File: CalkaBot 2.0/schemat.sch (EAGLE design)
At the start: 63 parts, among them IC1 TB6612FNG, IC2 LM339D, IC3 7806DT, Q1 16MHz

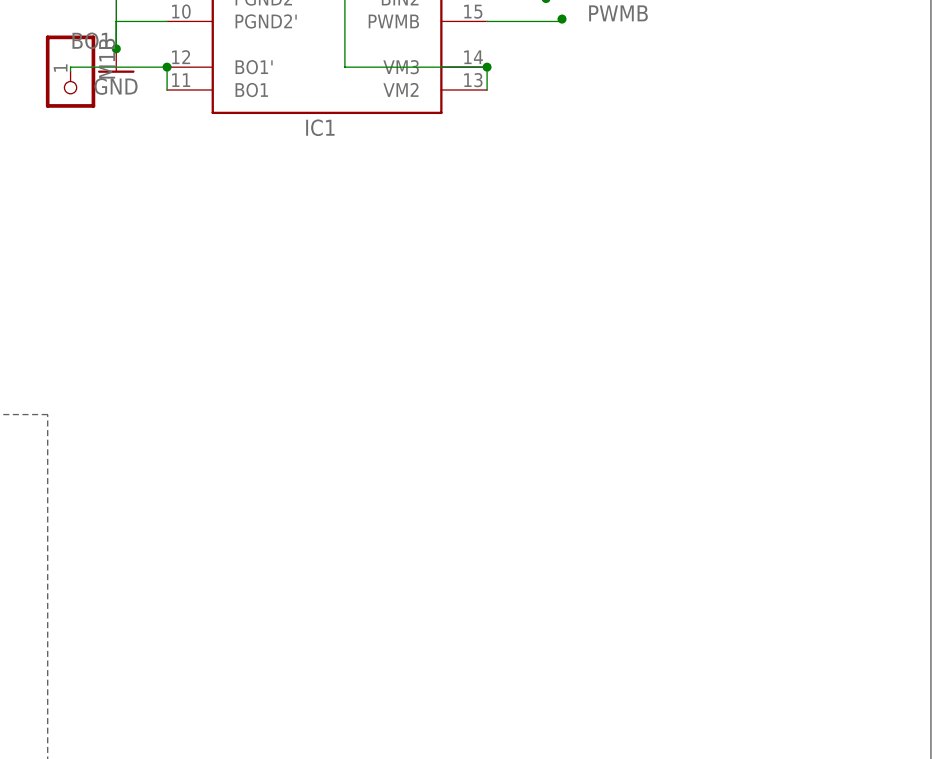
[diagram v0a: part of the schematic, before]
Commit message: dodane pinheady dla czujników odległości, teraz trzeba je podłączyć
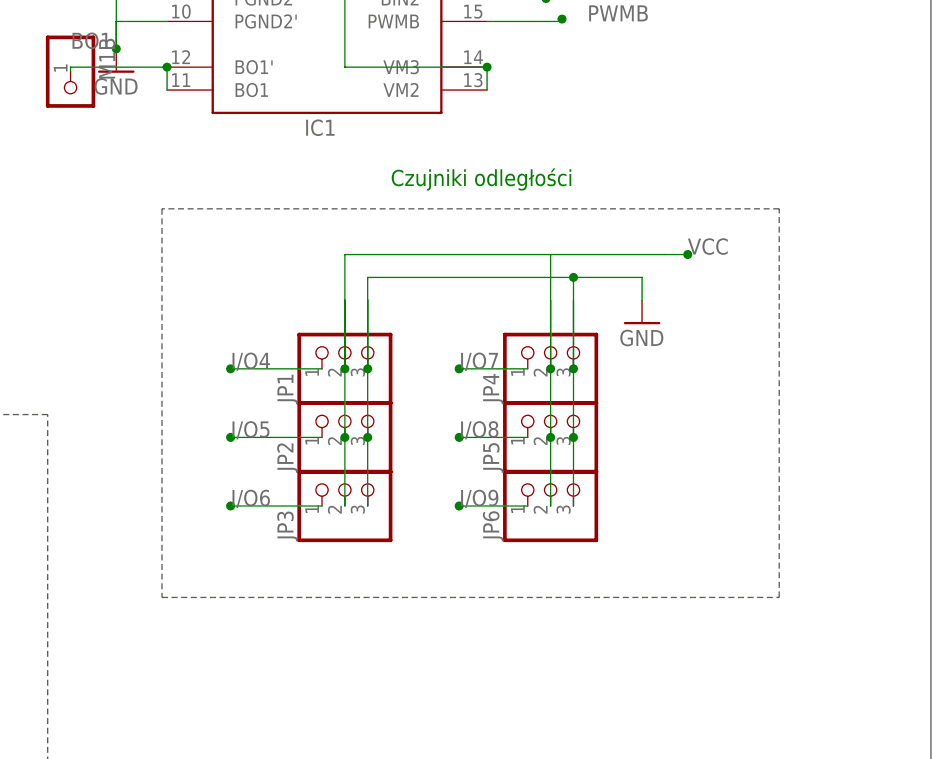
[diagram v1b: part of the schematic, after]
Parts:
- added JP1, JP2, JP3, JP4, JP5, JP6: (no value), pinhead:PINHD-1X3
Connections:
- net GND: now also JP1.3, JP2.3, JP3.3, JP4.3, JP5.3, JP6.3
- net I/O4: now also JP1.1
- net I/O5: now also JP2.1
- net I/O6: now also JP3.1
- net I/O7: now also JP4.1
- net I/O8: now also JP5.1
- net I/O9: now also JP6.1
- net VCC: now also JP1.2, JP2.2, JP3.2, JP4.2, JP5.2, JP6.2
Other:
- note added: "Czujniki odległości"
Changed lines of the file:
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@@
 <part name="L7" library="led" library_urn="urn:adsk.eagle:library:259" deviceset="LED" device="CHIP-LED0805" package3d_urn="urn:adsk.eagle:package:15818/2"/>
 <part name="GND24" library="supply1" library_urn="urn:adsk.eagle:library:371" deviceset="GND" device=""/>
+<part name="JP1" library="pinhead" library_urn="urn:adsk.eagle:library:325" deviceset="PINHD-1X3" device="" package3d_urn="urn:adsk.eagle:package:22458/2"/>
+<part name="JP2" library="pinhead" library_urn="urn:adsk.eagle:library:325" deviceset="PINHD-1X3" device="" package3d_urn="urn:adsk.eagle:package:22458/2"/>
+<part name="JP3" library="pinhead" library_urn="urn:adsk.eagle:library:325" deviceset="PINHD-1X3" device="" package3d_urn="urn:adsk.eagle:package:22458/2"/>
+<part name="JP4" library="pinhead" library_urn="urn:adsk.eagle:library:325" deviceset="PINHD-1X3" device="" package3d_urn="urn:adsk.eagle:package:22458/2"/>
+<part name="JP5" library="pinhead" library_urn="urn:adsk.eagle:library:325" deviceset="PINHD-1X3" device="" package3d_urn="urn:adsk.eagle:package:22458/2"/>
+<part name="JP6" library="pinhead" library_urn="urn:adsk.eagle:library:325" deviceset="PINHD-1X3" device="" package3d_urn="urn:adsk.eagle:package:22458/2"/>
+<part name="GND25" library="supply1" library_urn="urn:adsk.eagle:library:371" deviceset="GND" device=""/>
 </parts>
 <sheets>
@@
 <text x="50.8" y="152.4" size="6.4516" layer="91">zasilanie</text>
 <text x="-33.02" y="170.18" size="1.778" layer="91">Dioda w pionie cyfrowym</text>
+<text x="99.06" y="33.02" size="1.778" layer="91">Czujniki odległości</text>
 </plain>
 <instances>
@@
 <attribute name="VALUE" x="-12.7" y="144.78" size="1.778" layer="96"/>
 </instance>
+<instance part="JP1" gate="A" x="93.98" y="15.24" smashed="yes" rot="R90">
+<attribute name="NAME" x="88.265" y="8.89" size="1.778" layer="95" rot="R90"/>
+<attribute name="VALUE" x="101.6" y="8.89" size="1.778" layer="96" rot="R90"/>
+</instance>
+<instance part="JP2" gate="A" x="93.98" y="7.62" smashed="yes" rot="R90">
+<attribute name="NAME" x="88.265" y="1.27" size="1.778" layer="95" rot="R90"/>
+<attribute name="VALUE" x="101.6" y="1.27" size="1.778" layer="96" rot="R90"/>
+</instance>
+<instance part="JP3" gate="A" x="93.98" y="0" smashed="yes" rot="R90">
+<attribute name="NAME" x="88.265" y="-6.35" size="1.778" layer="95" rot="R90"/>
+<attribute name="VALUE" x="101.6" y="-6.35" size="1.778" layer="96" rot="R90"/>
+</instance>
+<instance part="JP4" gate="A" x="116.84" y="15.24" smashed="yes" rot="R90">
+<attribute name="NAME" x="111.125" y="8.89" size="1.778" layer="95" rot="R90"/>
+<attribute name="VALUE" x="124.46" y="8.89" size="1.778" layer="96" rot="R90"/>
+</instance>
+<instance part="JP5" gate="A" x="116.84" y="7.62" smashed="yes" rot="R90">
+<attribute name="NAME" x="111.125" y="1.27" size="1.778" layer="95" rot="R90"/>
+<attribute name="VALUE" x="124.46" y="1.27" size="1.778" layer="96" rot="R90"/>
+</instance>
+<instance part="JP6" gate="A" x="116.84" y="0" smashed="yes" rot="R90">
+<attribute name="NAME" x="111.125" y="-6.35" size="1.778" layer="95" rot="R90"/>
+<attribute name="VALUE" x="124.46" y="-6.35" size="1.778" layer="96" rot="R90"/>
+</instance>
+<instance part="GND25" gate="1" x="127" y="17.78" smashed="yes">
+<attribute name="VALUE" x="124.46" y="15.24" size="1.778" layer="96"/>
+</instance>
 </instances>
 <busses>
@@
 <wire x1="0" y1="119.38" x2="0" y2="167.64" width="0.762" layer="92" style="shortdash"/>
 <wire x1="0" y1="167.64" x2="-43.18" y2="167.64" width="0.762" layer="92" style="shortdash"/>
+</segment>
+</bus>
+<bus name="B$8">
+<segment>
+<wire x1="73.66" y1="30.48" x2="73.66" y2="-12.7" width="0.762" layer="92" style="dashdot"/>
+<wire x1="73.66" y1="-12.7" x2="142.24" y2="-12.7" width="0.762" layer="92" style="dashdot"/>
+<wire x1="142.24" y1="-12.7" x2="142.24" y2="30.48" width="0.762" layer="92" style="dashdot"/>
+<wire x1="142.24" y1="30.48" x2="73.66" y2="30.48" width="0.762" layer="92" style="dashdot"/>
 </segment>
 </bus>
@@
 <wire x1="-10.82" y1="154.42" x2="-10.16" y2="154.42" width="0.1524" layer="91"/>
 <wire x1="-10.16" y1="154.42" x2="-10.16" y2="149.86" width="0.1524" layer="91"/>
+</segment>
+<segment>
+<pinref part="JP6" gate="A" pin="3"/>
+<pinref part="JP5" gate="A" pin="3"/>
+<wire x1="119.38" y1="-2.54" x2="119.38" y2="5.08" width="0.1524" layer="91"/>
+<pinref part="JP4" gate="A" pin="3"/>
+<wire x1="119.38" y1="5.08" x2="119.38" y2="12.7" width="0.1524" layer="91"/>
+<junction x="119.38" y="5.08"/>
+<wire x1="119.38" y1="12.7" x2="119.38" y2="20.32" width="0.1524" layer="91"/>
+<junction x="119.38" y="12.7"/>
+<wire x1="119.38" y1="12.7" x2="119.38" y2="22.86" width="0.1524" layer="91"/>
+<wire x1="119.38" y1="22.86" x2="127" y2="22.86" width="0.1524" layer="91"/>
+<wire x1="127" y1="22.86" x2="127" y2="20.32" width="0.1524" layer="91"/>
+<pinref part="GND25" gate="1" pin="GND"/>
+<pinref part="JP3" gate="A" pin="3"/>
+<pinref part="JP2" gate="A" pin="3"/>
+<wire x1="96.52" y1="-2.54" x2="96.52" y2="5.08" width="0.1524" layer="91"/>
+<pinref part="JP1" gate="A" pin="3"/>
+<wire x1="96.52" y1="5.08" x2="96.52" y2="12.7" width="0.1524" layer="91"/>
+<junction x="96.52" y="5.08"/>
+<wire x1="96.52" y1="12.7" x2="96.52" y2="20.32" width="0.1524" layer="91"/>
+<junction x="96.52" y="12.7"/>
+<wire x1="96.52" y1="12.7" x2="96.52" y2="22.86" width="0.1524" layer="91"/>
+<wire x1="96.52" y1="22.86" x2="119.38" y2="22.86" width="0.1524" layer="91"/>
+<junction x="119.38" y="22.86"/>
 </segment>
 </net>
@@
 <label x="-73.66" y="86.36" size="1.778" layer="95"/>
 </segment>
+<segment>
+<pinref part="JP4" gate="A" pin="2"/>
+<wire x1="116.84" y1="12.7" x2="116.84" y2="20.32" width="0.1524" layer="91"/>
+<pinref part="JP5" gate="A" pin="2"/>
+<wire x1="116.84" y1="12.7" x2="116.84" y2="5.08" width="0.1524" layer="91"/>
+<junction x="116.84" y="12.7"/>
+<pinref part="JP6" gate="A" pin="2"/>
+<wire x1="116.84" y1="-2.54" x2="116.84" y2="5.08" width="0.1524" layer="91"/>
+<junction x="116.84" y="5.08"/>
+<wire x1="116.84" y1="12.7" x2="116.84" y2="25.4" width="0.1524" layer="91"/>
+<wire x1="116.84" y1="25.4" x2="129.54" y2="25.4" width="0.1524" layer="91"/>
+<junction x="132.08" y="25.4"/>
+<label x="132.08" y="25.4" size="1.778" layer="95"/>
+<pinref part="JP1" gate="A" pin="2"/>
+<pinref part="JP2" gate="A" pin="2"/>
+<wire x1="129.54" y1="25.4" x2="132.08" y2="25.4" width="0.1524" layer="91"/>
+<wire x1="93.98" y1="12.7" x2="93.98" y2="5.08" width="0.1524" layer="91"/>
+<pinref part="JP3" gate="A" pin="2"/>
+<wire x1="93.98" y1="5.08" x2="93.98" y2="-2.54" width="0.1524" layer="91"/>
+<junction x="93.98" y="5.08"/>
+<wire x1="93.98" y1="12.7" x2="93.98" y2="20.32" width="0.1524" layer="91"/>
+<junction x="93.98" y="12.7"/>
+<wire x1="93.98" y1="12.7" x2="93.98" y2="25.4" width="0.1524" layer="91"/>
+<wire x1="93.98" y1="25.4" x2="116.84" y2="25.4" width="0.1524" layer="91"/>
+</segment>
 </net>
 <net name="BIN1" class="0">
@@
 <label x="25.2" y="41.8" size="1.778" layer="95"/>
 </segment>
+<segment>
+<pinref part="JP6" gate="A" pin="1"/>
+<wire x1="114.3" y1="-2.54" x2="106.68" y2="-2.54" width="0.1524" layer="91"/>
+<junction x="106.68" y="-2.54"/>
+<label x="106.68" y="-2.54" size="1.778" layer="95"/>
+</segment>
 </net>
 <net name="I/O8" class="0">
@@
 <label x="24.9" y="44.3" size="1.778" layer="95"/>
 </segment>
+<segment>
+<pinref part="JP5" gate="A" pin="1"/>
+<wire x1="114.3" y1="5.08" x2="106.68" y2="5.08" width="0.1524" layer="91"/>
+<junction x="106.68" y="5.08"/>
+<label x="106.68" y="5.08" size="1.778" layer="95"/>
+</segment>
 </net>
 <net name="I/O7" class="0">
@@
 <junction x="21.3" y="46.9"/>
 <label x="24.5" y="46.8" size="1.778" layer="95"/>
+</segment>
+<segment>
+<pinref part="JP4" gate="A" pin="1"/>
+<wire x1="114.3" y1="12.7" x2="106.68" y2="12.7" width="0.1524" layer="91"/>
+<junction x="106.68" y="12.7"/>
+<label x="106.68" y="12.7" size="1.778" layer="95"/>
 </segment>
 </net>
@@
 <label x="22.86" y="99.06" size="1.778" layer="95"/>
 </segment>
+<segment>
+<pinref part="JP1" gate="A" pin="1"/>
+<wire x1="91.44" y1="12.7" x2="81.28" y2="12.7" width="0.1524" layer="91"/>
+<junction x="81.28" y="12.7"/>
+<label x="81.28" y="12.7" size="1.778" layer="95"/>
+</segment>
 </net>
 <net name="I/O5" class="0">
@@
 <label x="22.86" y="96.52" size="1.778" layer="95"/>
 </segment>
+<segment>
+<pinref part="JP2" gate="A" pin="1"/>
+<wire x1="91.44" y1="5.08" x2="81.28" y2="5.08" width="0.1524" layer="91"/>
+<junction x="81.28" y="5.08"/>
+<label x="81.28" y="5.08" size="1.778" layer="95"/>
+</segment>
 </net>
 <net name="I/O6" class="0">
@@
 <label x="22.86" y="93.98" size="1.778" layer="95"/>
 </segment>
-</net>
+<segment>
+<pinref part="JP3" gate="A" pin="1"/>
+<wire x1="91.44" y1="-2.54" x2="81.28" y2="-2.54" width="0.1524" layer="91"/>
+<junction x="81.28" y="-2.54"/>
+<label x="81.28" y="-2.54" size="1.778" layer="95"/>
+</segment>
+</net>
